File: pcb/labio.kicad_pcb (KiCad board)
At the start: 2 copper layers, 150 x 100 mm, 178 parts, among them IC201 AT24CS32-XHM, J701 JACK_TRRS_6PINS, P1 CONN_02X20, P301 CONN_01X04, P302 CONN_01X04, P303 CONN_01X04, P401 CONN_01X12, P601 CONN_01X02, P602 CONN_01X02, P603 CONN_01X04, P604 CONN_01X02, P605 CONN_01X03, P606 CONN_01X03, P607 CONN_01X05, P608 CONN_01X05, P701 CONN_01X04, P702 CONN_01X04, P703 CONN_01X04, P704 CONN_01X02, P901 CONN_01X06, Q301 PHOTOTRANSISTOR, Q601 Q_NMOS_GSD, Q602 Q_NMOS_GSD, Q603 Q_NMOS_GSD, Q604 Q_NMOS_GSD, Q605 Q_NMOS_GSD, Q606 Q_NMOS_GSD, Q607 Q_NMOS_GSD, Q608 Q_NMOS_GSD, Q609 Q_NMOS_GSD, Q610 Q_NMOS_GSD, Q611 Q_NMOS_GSD, Q612 Q_NMOS_GSD, Q613 Q_NMOS_GSD, SW301 DIP_SWITCH_X04, SW401 DIP_SWITCH_X04, SW501 DIP_SWITCH_X04, SW601 DIP_SWITCH_X04, SW602 DIP_SWITCH_X04, SW603 DIP_SWITCH_X04, SW604 DIP_SWITCH_X04, SW605 ROT_ENC, SW606 DIP_SWITCH_X04, SW701 DIP_SWITCH_X04, SW702 DIP_SWITCH_X04, SW801 SW_PUSH, SW802 SW_PUSH, SW803 SW_PUSH, SW804 SW_PUSH, SW805 SW_PUSH, U201 AP7365_SOT-23-5, U301 ADS1015, U501 LSM303, U502 BMP180, U601 L298P, U701 SPU0410HR5H, U702 WM8731

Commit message: floorplan on 150x85mm board, use al caps for motors
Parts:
- added C608: 47uF, Capacitors_SMD:c_elec_6.3x5.8, F.Cu at (185.5, 124.0)
- added C609: 47uF, Capacitors_SMD:c_elec_6.3x5.8, F.Cu at (185.5, 115.5)
- C501, C702, C706, C712, C716, C718: value 10uF -> 4.7uF; footprint Capacitors_Tantalum_SMD:TantalC_SizeA_EIA-3216_Wave -> Capacitors_SMD:C_0603
- C603, C604: value 10uF -> 47uF; footprint Capacitors_Tantalum_SMD:TantalC_SizeA_EIA-3216_Wave -> Capacitors_SMD:c_elec_6.3x5.8
- IC201, R203, R204, R205, W201, W202: moved to B.Cu
- moved D610 286.2 mm to (185.5, 108.0), turned to 180 degrees
- moved R624 268.8 mm to (189.0, 108.0)
- moved C601 264.9 mm to (168.5, 123.0), turned to 270 degrees
- moved D601 262.2 mm to (181.5, 108.0)
- moved R607 257.0 mm to (181.5, 105.5), turned to 180 degrees
- moved R609 249.3 mm to (167.0, 101.5), turned to 90 degrees
- moved R601 244.5 mm to (158.0, 101.5), turned to 90 degrees
- moved D611 236.9 mm to (189.9, 104.8)
- moved D612 236.9 mm to (187.3, 104.8)
- moved D613 236.9 mm to (184.8, 104.8)
- moved SW603 236.5 mm to (189.9, 92.1)
- moved R608 235.2 mm to (164.0, 101.5), turned to 90 degrees
- moved R602 232.0 mm to (161.0, 101.5), turned to 90 degrees
- moved P603 229.6 mm to (175.9, 104.8)
- moved C605 229.2 mm to (126.5, 108.0), turned to 90 degrees
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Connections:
- IC201 pad 5: /labio-rpi/RPI_ID_SD -> /labio-rpi/ID_SD
- IC201 pad 6: /labio-rpi/RPI_ID_SC -> /labio-rpi/ID_SC
- R204 pad 2: /labio-rpi/RPI_ID_SD -> /labio-rpi/ID_SD
- R205 pad 2: /labio-rpi/RPI_ID_SC -> /labio-rpi/ID_SC
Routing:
- net /labio-rpi/3V3_2: track 0.00 -> 32.4 mm
- net /labio-rpi/ID_SD: track 0.00 -> 18.4 mm
- net /labio-rpi/ID_SC: track 0.00 -> 13.6 mm
- net Net-(IC201-Pad7): track 0.00 -> 3.25 mm
- added copper zone on F.Cu, net /labio-dio/VS_MOTOR
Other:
- board size 150 x 100 mm -> 150 x 85 mm
- net class Default: trace_width 0.25 -> 0.254; via_dia 0.6 -> 0.6096; via_drill 0.4 -> 0.3048
- board text added: "AIN0"
- board text added: "AIN1"
- board text added: "AIN2"
- board text added: "AIN3"

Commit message: first pass routing, fixed audio header 3v3 net
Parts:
- C501, C702, C706, C712, C716, C718: footprint Capacitors_SMD:C_0603 -> Capacitors_SMD:C_0805
- C801, C802, C803, C804, C805: value depop -> dnp
- moved R402 16.0 mm to (223.2, 71.2), turned to 270 degrees
- moved R403 15.9 mm to (228.2, 71.2), turned to 270 degrees
- moved R401 15.6 mm to (225.8, 71.2), turned to 90 degrees
- moved R611 15.5 mm to (151.5, 80.2)
- moved Q604 15.2 mm to (151.5, 77.0)
- moved R613 14.9 mm to (151.5, 73.5)
- moved D605 14.6 mm to (151.5, 71.0)
- moved R701 13.6 mm to (223.5, 104.5), turned to 180 degrees
- moved D701 11.6 mm to (220.0, 104.5), turned to 180 degrees
- moved R603 11.5 mm to (164.2, 80.2)
- moved Q601 11.0 mm to (164.2, 77.0)
- moved R605 10.6 mm to (164.3, 73.5)
- moved P605 10.2 mm to (184.8, 132.8)
- moved P606 10.2 mm to (174.6, 132.8)
- moved D602 10.1 mm to (164.3, 71.0)
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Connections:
- P702 pad 1: /labio-audio/VDD_3V3_J -> /labio-audio/VDD3V3_J
- P702 pad 2: /labio-audio/VDD_3V3_J -> /labio-audio/VDD3V3_J
- P702 pad 3: /labio-audio/VDD_3V3_J -> /labio-audio/VDD3V3_J
- P702 pad 4: /labio-audio/VDD_3V3_J -> /labio-audio/VDD3V3_J
- SW701 pad 1: (no net) -> /labio-rpi/3V3_EXTRA
- SW803 pad 2: Net-(SW803-Pad2) -> GND
- SW804 pad 2: Net-(SW804-Pad2) -> GND
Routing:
- net /labio-dpad/DPAD_RIGHT: track 0.00 -> 257.3 mm, vias 0 -> 9
- net /labio-dpad/DPAD_CENTER: track 0.00 -> 255.6 mm, vias 0 -> 8
- net /labio-dpad/DPAD_DOWN: track 0.00 -> 255.1 mm, vias 0 -> 9
- net /labio-dpad/DPAD_LEFT: track 0.00 -> 242.1 mm, vias 0 -> 8
- net /labio-dpad/DPAD_UP: track 0.00 -> 229.6 mm, vias 0 -> 8
- net /labio-rpi/VBUS: track 0.00 -> 176.5 mm, vias 0 -> 8
- net /labio-rpi/3V3_EXTRA: track 0.00 -> 160.1 mm, vias 0 -> 8
- net /labio-rpi/GPIO1_SDA1: track 0.00 -> 154.9 mm, vias 0 -> 2
- net /labio-rpi/GPIO3_SCL1: track 0.00 -> 151.3 mm, vias 0 -> 3
- net GND: track 0.00 -> 150.6 mm, vias 0 -> 90
- net /labio-adc/ALERT: track 0.00 -> 149.2 mm, vias 0 -> 11
- net /labio-rpi/GPIO21_PCM_DOUT: track 0.00 -> 142.6 mm, vias 0 -> 4
- net /labio-audio/BCLK: track 0.00 -> 139.7 mm, vias 0 -> 5
- net /labio-rpi/GPIO12_PWM0: track 0.00 -> 139.0 mm, vias 0 -> 5
- net /labio-rpi/GPIO20_PCM_DIN: track 0.00 -> 137.6 mm, vias 0 -> 4
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- added copper zone on F.Cu, net /labio-audio/VDD3V3_J
- added copper zone on F.Cu, net /labio-dio/VDD_SERVO
- added copper zone on B.Cu, net GND
- added copper zone on B.Cu, net GNDA
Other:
- outline, holes or cut-outs redrawn
- net class 10/10 added: clearance 0.254, trace_width 0.254, via_dia 0.6096, via_drill 0.3048
- net class Default: clearance 0.2 -> 0.2032
- net class Motors added: clearance 0.254, trace_width 0.508, via_dia 0.6096, via_drill 0.3048
- net class Power added: clearance 0.254, trace_width 0.381, via_dia 0.6096, via_drill 0.3048
- rule trace_clearance: 0.2 -> 0.2032
- rule trace_min: 0.2 -> 0.254
- board text added: "BCLK"
- board text added: "DPad C"
- board text added: "DPad D"
- board text added: "DPad L"
- board text added: "DPad R"
- board text added: "DPad U"
- board text added: "Enc 0 A"
- board text added: "Enc 0 B"
- board text added: "Enc 0 I"
- board text added: "Enc 1 A"
- board text added: "Enc 1 B"
- board text added: "Enc 1 I"
- board text added: "GPIO 12"
- board text added: "GPIO 13"
- board text added: "GPIO 16"
- board text added: "GPIO 17"
- board text added: "GPIO 18"
- board text added: "GPIO 19"
- board text added: "GPIO 20"
- board text added: "GPIO 21"
- board text added: "GPIO 23"
- board text added: "GPIO 26"
- board text added: "GPIO 6"
- board text added: "GPIO 7"
- board text added: "I2C Int"
- board text added: "LRCLK"
- board text added: "Motor 1"
- board text added: "Motor 2"
- board text added: "Motor 3"
- board text added: "Motor 4"
- board text added: "PWM 0"
- board text added: "PWM 1"
- board text added: "SDIN"
- board text added: "SDOUT"
- board text removed: "Mot1"
- board text removed: "Mot2"

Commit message: update imu parts, adc rails, motor headers
* replace LSM303C accelerometer with LSM303D for better sensor ranges at same cost.
* add L3GD20H gyroscope so we have a 10-DOF imu. consider leaving depopulated for complexity.
* add 0 ohms to accel/gyro address and interrupt pins in case of later changes
* change ADC rails to 5V to read 5V power shunts. add level shifters to the 3.3V I2C bus.
* use 3.5mm pitch headers for motor terminal blocks to accept higher guage wire.

todo:
* redo ADC routing
* make space behind motor headers
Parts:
- added C507: 4.7uF, Capacitors_SMD:C_0805, F.Cu at (124.8, 68.0)
- added C508: 4.7uF, Capacitors_SMD:C_0805, F.Cu at (115.2, 52.0)
- added C509: 4.7uF, Capacitors_SMD:C_0805, F.Cu at (115.2, 68.0)
- added C510: 0.1uF, Capacitors_SMD:C_0603, F.Cu at (115.2, 54.5)
- added C511: 0.1uF, Capacitors_SMD:C_0603, F.Cu at (115.2, 65.5)
- added C512: 0.01uF 25V, Capacitors_SMD:C_0603, F.Cu at (115.2, 57.0)
- added C513: 0.22uF, Capacitors_SMD:C_0603, F.Cu at (128.2, 57.0)
- added Q302: Q_NMOS_GSD, TO_SOT_Packages_SMD:SOT-23, F.Cu at (135.9, 41.6)
- added Q303: Q_NMOS_GSD, TO_SOT_Packages_SMD:SOT-23, F.Cu at (139.8, 41.6)
- added R303: 10k, Resistors_SMD:R_0603, F.Cu at (136.0, 46.0)
- added R304: 10k, Resistors_SMD:R_0603, F.Cu at (139.5, 45.5)
- added R502: 0, Resistors_SMD:R_0603, F.Cu at (120.0, 52.0)
- added R503: dnp-0, Resistors_SMD:R_0603, F.Cu at (120.0, 54.5)
- added R504: 0, Resistors_SMD:R_0603, F.Cu at (120.0, 57.0)
- added R505: 0, Resistors_SMD:R_0603, F.Cu at (111.8, 57.0)
- added R506: 0, Resistors_SMD:R_0603, F.Cu at (128.2, 68.0)
- added R507: 0, Resistors_SMD:R_0603, F.Cu at (111.8, 52.0)
- added R508: 0, Resistors_SMD:R_0603, F.Cu at (128.2, 65.5)
- added R509: 0, Resistors_SMD:R_0603, F.Cu at (128.2, 70.5)
- added R510: 0, Resistors_SMD:R_0603, F.Cu at (111.8, 65.5)
- added R511: 0, Resistors_SMD:R_0603, F.Cu at (111.8, 54.5)
- added R512: dnp-0, Resistors_SMD:R_0603, F.Cu at (128.2, 54.5)
- added R513: 0, Resistors_SMD:R_0603, F.Cu at (128.2, 52.0)
- added R514: dnp-0, Resistors_SMD:R_0603, F.Cu at (111.8, 68.0)
- added R515: 0, Resistors_SMD:R_0603, F.Cu at (111.8, 70.5)
- added U503: L3GD20H, labio-special:LGA-16_3x3mm_Pitch0.5mm_ST, F.Cu at (113.5, 61.2)
- C505: value 0.1uF -> 4.7uF; footprint Capacitors_SMD:C_0603 -> Capacitors_SMD:C_0805
- P601, P602, P604: footprint Pin_Headers:Pin_Header_Straight_1x02 -> labio-special:Pin_Header_Straight_1x02_Pitch3.5mm
- U501: value LSM303 -> LSM303D; footprint labio-special:LSM303-LGA-12 -> labio-special:LGA-16_3x3mm_Pitch0.5mm_ST
- U502: value BMP180 -> BMP280; footprint labio-special:BMP180-LGA-7 -> labio-special:LGA-8_2.5x2.0mm_Pitch0.65mm_BMx280
- moved R501 17.4 mm to (128.2, 75.2)
- moved D501 16.9 mm to (128.2, 72.8)
- moved C501 13.5 mm to (124.8, 52.0), turned to 180 degrees
- moved C503 12.9 mm to (124.8, 54.5), turned to 180 degrees
- moved R201 12.5 mm to (109.8, 73.2), turned to 90 degrees
- moved U501 10.4 mm to (126.5, 61.2), turned to 90 degrees
- moved R202 10.0 mm to (112.2, 73.2), turned to 90 degrees
- moved C506 9.42 mm to (119.0, 64.8), turned to 270 degrees
- moved C505 7.16 mm to (124.5, 57.2)
- moved C504 6.91 mm to (121.0, 64.8), turned to 270 degrees
- moved U502 4.51 mm to (120.0, 60.8)
- moved C502 2.93 mm to (124.8, 65.5), turned to 0 degrees
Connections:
- C301 pad 1: /labio-adc/VDD_J -> /labio-adc/VDD5V_J
- D301 pad 2: /labio-adc/VDD_J -> /labio-adc/VDD5V_J
- P302 pad 1: /labio-adc/VDD_J -> /labio-adc/VDD5V_J
- P302 pad 2: /labio-adc/VDD_J -> /labio-adc/VDD5V_J
- P302 pad 3: /labio-adc/VDD_J -> /labio-adc/VDD5V_J
- P302 pad 4: /labio-adc/VDD_J -> /labio-adc/VDD5V_J
- R301 pad 1: /labio-adc/VDD_J -> (no net)
- SW301 pad 1: /labio-adc/VDD_J -> /labio-adc/VDD5V_J
- SW301 pad 8: /labio-rpi/3V3_EXTRA -> (no net)
- U301 pad 1: /labio-adc/VDD_J -> /labio-adc/VDD5V_J
- U301 pad 10: /labio-adc/SCL_J -> Net-(Q302-Pad3)
- U301 pad 8: /labio-adc/VDD_J -> /labio-adc/VDD5V_J
- U301 pad 9: /labio-adc/SDA_J -> Net-(Q303-Pad3)
- U501 pad 1: /labio-imu/SCL_J -> /labio-imu/VDD3V3_J
- U501 pad 10: /labio-imu/VDD3V3_J -> GND
- U501 pad 11: (no net) -> /labio-imu/ACCEL_INT1
- U501 pad 12: /labio-imu/INT_J -> GND
- U501 pad 2: /labio-imu/VDD3V3_J -> Net-(C513-Pad1)
- U501 pad 3: /labio-imu/VDD3V3_J -> Net-(C513-Pad2)
- U501 pad 4: /labio-imu/SDA_J -> /labio-imu/SCL_J
- U501 pad 5: Net-(C505-Pad1) -> GND
- U501 pad 6: GND -> /labio-imu/SDA_J
- U501 pad 7: /labio-imu/INT_J -> /labio-imu/ACCEL_SA0
- U501 pad 8: GND -> /labio-imu/ACCEL_CS
- U501 pad 9: /labio-imu/VDD3V3_J -> /labio-imu/ACCEL_INT2
- U502 pad 1: (no net) -> GND
- U502 pad 2: /labio-imu/VDD3V3_J -> /labio-imu/BMP_CS
- U502 pad 3: /labio-imu/VDD3V3_J -> /labio-imu/SDA_J
- U502 pad 4: (no net) -> /labio-imu/SCL_J
- U502 pad 5: /labio-imu/SCL_J -> /labio-imu/BMP_ADDR
- U502 pad 6: /labio-imu/SDA_J -> /labio-imu/VDD3V3_J
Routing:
- net /labio-imu/INT_J: track 10.3 -> 58.9 mm, vias 2 -> 0
- net /labio-adc/VDD_J: track 38.0 -> 0.00 mm, vias 2 -> 0
- net /labio-adc/VDD5V_J: track 0.00 -> 38.0 mm, vias 0 -> 2
- net /labio-imu/VDD3V3_J: track 34.8 -> 0.00 mm
- net GND: track 150.6 -> 172.1 mm, vias 90 -> 105
- net /labio-imu/SDA_J: track 23.1 -> 36.3 mm, vias 0 -> 4
- net /labio-imu/GYRO_INT2: track 0.00 -> 11.9 mm
- net /labio-rpi/3V3_1: track 15.8 -> 27.3 mm
- net /labio-imu/ACCEL_SA0: track 0.00 -> 10.8 mm
- net /labio-imu/GYRO_SA0: track 0.00 -> 8.68 mm
- net /labio-imu/ACCEL_INT1: track 0.00 -> 8.30 mm
- net /labio-imu/BMP_ADDR: track 0.00 -> 8.20 mm
- net /labio-imu/BMP_CS: track 0.00 -> 8.15 mm
- net /labio-imu/GYRO_INT1: track 0.00 -> 8.13 mm
- net /labio-imu/ACCEL_INT2: track 0.00 -> 5.83 mm
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- added copper zone on F.Cu, net /labio-imu/VDD3V3_J

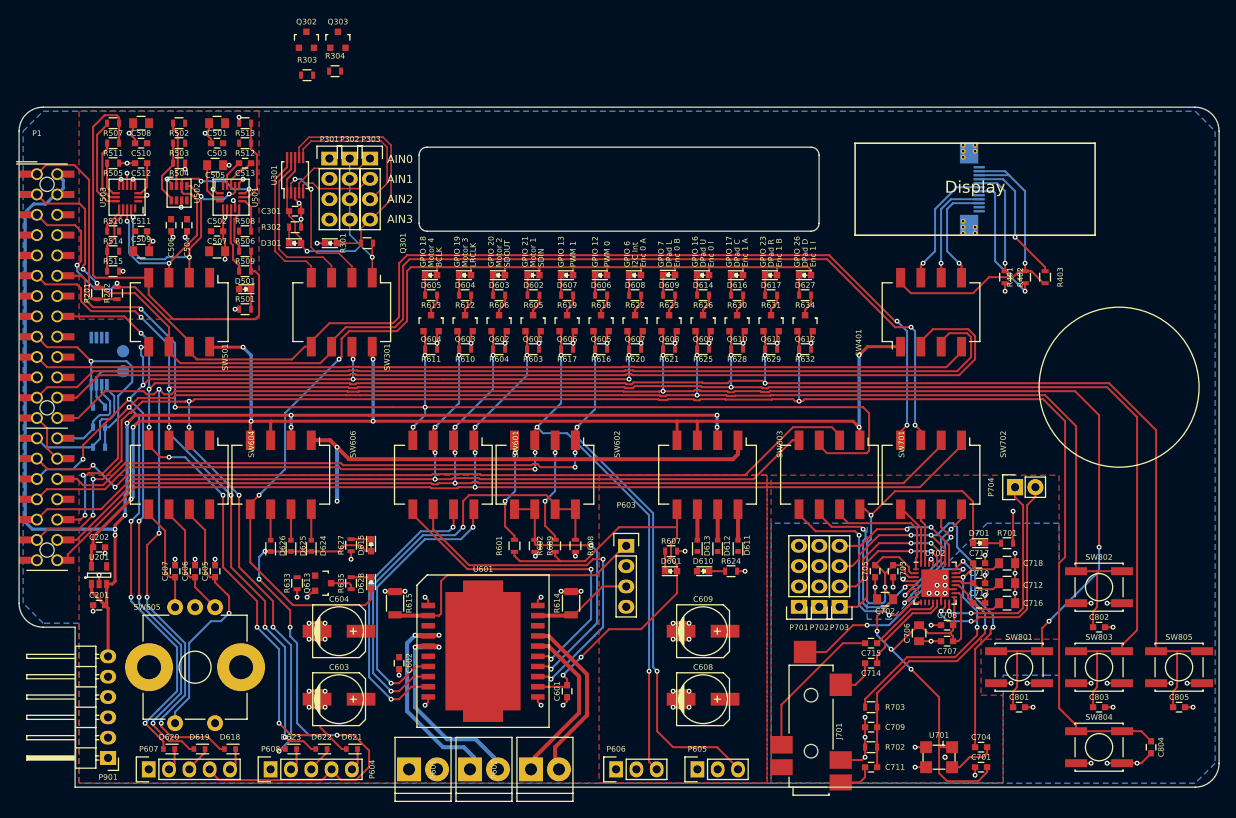
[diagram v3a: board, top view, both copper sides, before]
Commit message: finish rerouting for new parts
* fix adc power supply nets
* redo adc layout
* move motor controller up to make space for headers
* add motor controller heatsink mount
* fix motor controller ground pad net

todo:
* silkscreen
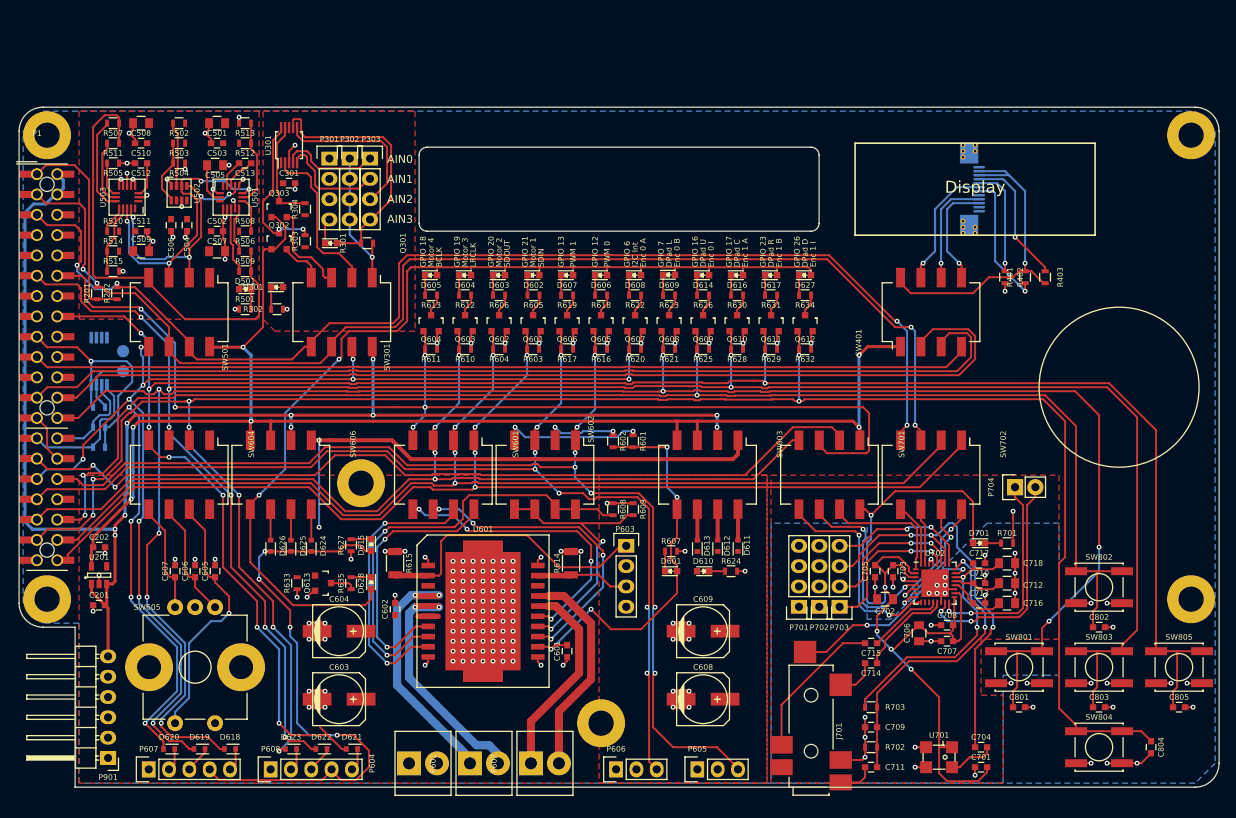
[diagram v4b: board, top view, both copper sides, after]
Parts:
- added H1001: hole, labio-special:hole-m3, F.Cu at (103.5, 53.5)
- added H1002: hole, labio-special:hole-m3, F.Cu at (142.8, 97.0)
- added H1003: hole, labio-special:hole-m3, F.Cu at (246.5, 53.5)
- added H1004: hole, labio-special:hole-m3, F.Cu at (246.5, 111.5)
- added H1005: hole, labio-special:hole-m3, F.Cu at (103.5, 111.5)
- added H1006: hole, labio-special:hole-m3, F.Cu at (172.8, 127.0)
- U601: value L298P -> L298P_PowerSO20
- moved Q302 25.4 mm to (132.5, 66.8)
- moved Q303 22.4 mm to (132.5, 62.8)
- moved R303 20.8 mm to (135.8, 66.8), turned to 90 degrees
- moved R601 19.8 mm to (176.8, 91.8)
- moved R304 17.7 mm to (135.8, 62.8), turned to 90 degrees
- moved R602 15.0 mm to (174.2, 91.8)
- moved R609 13.1 mm to (176.8, 100.2), turned to 90 degrees
- moved R302 10.5 mm to (132.2, 75.2)
- moved C602 6.77 mm to (147.0, 112.8), turned to 90 degrees
- moved R608 6.57 mm to (174.2, 100.2), turned to 90 degrees
- moved D301 5.94 mm to (132.2, 72.5)
- moved C601 5.00 mm to (168.5, 118.0)
- moved R614 5.00 mm to (169.0, 107.0)
- moved R615 5.00 mm to (147.0, 107.0)
- moved U601 5.00 mm to (158.0, 113.0)
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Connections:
- net Net-(Q302-Pad3) renamed /labio-adc/SCL_5V
- net Net-(Q303-Pad3) renamed /labio-adc/SDA_5V
- Q302 pad 1: /labio-adc/VDD3V3 -> /labio-rpi/3V3_EXTRA
- Q303 pad 1: /labio-adc/VDD3V3 -> /labio-rpi/3V3_EXTRA
- R301 pad 1: (no net) -> /labio-adc/VDD5V_J
- SW301 pad 8: (no net) -> /labio-rpi/VBUS
- U601 pad 21: (no net) -> GND
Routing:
- net GND: track 172.1 -> 270.7 mm, vias 105 -> 181
- net /labio-adc/SCL_5V: track 1.20 -> 19.7 mm, vias 0 -> 2
- net /labio-adc/VDD5V_J: track 38.0 -> 21.9 mm, vias 2 -> 1
- net /labio-adc/SCL_J: track 17.8 -> 5.53 mm
- net /labio-adc/SDA_5V: track 1.45 -> 13.1 mm
- net /labio-rpi/3V3_EXTRA: track 160.1 -> 170.9 mm, vias 8 -> 6
- net /labio-rpi/VBUS: track 176.5 -> 185.1 mm, vias 8 -> 10
- net /labio-dio/VDD_MOT: track 59.2 -> 50.9 mm, vias 2 -> 4
- net /labio-adc/SDA_J: track 19.5 -> 11.6 mm
- net /labio-dio/VS_MOTOR: track 63.1 -> 69.7 mm
- net /labio-dio/MOT_IN3_J: track 45.4 -> 38.9 mm, vias 2 -> 4
- net /labio-dio/MOTOR_OUT4: track 21.7 -> 27.3 mm
- net /labio-dio/MOTOR_OUT3: track 20.6 -> 25.6 mm
- net Net-(R601-Pad2): track 13.5 -> 17.7 mm
- net /labio-dio/MOTOR_OUT2: track 27.6 -> 31.5 mm
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- added copper zone on F.Cu, net /labio-adc/VDD5V_J
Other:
- net class Motors: trace_width 0.508 -> 1.016
